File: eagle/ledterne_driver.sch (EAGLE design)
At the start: 15 parts, among them IC1 MEGA8-AI

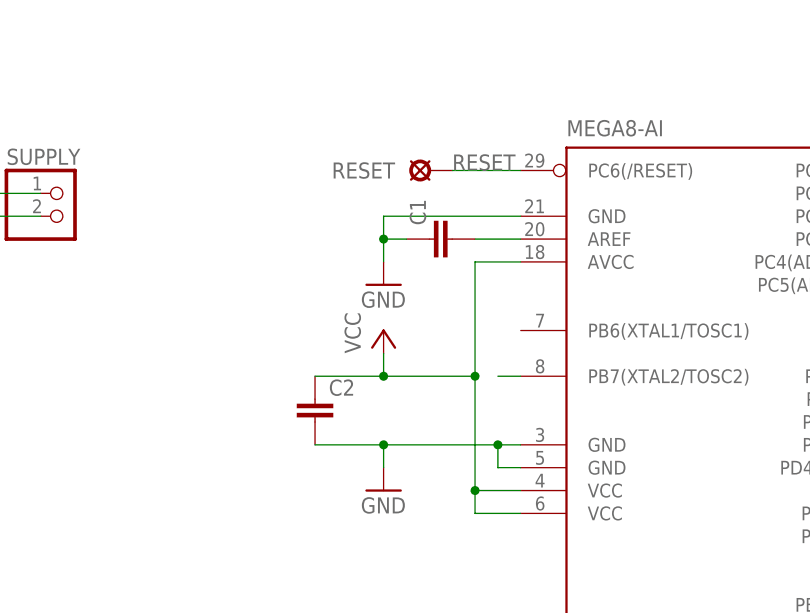
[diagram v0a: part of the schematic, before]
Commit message: Add capacitor values
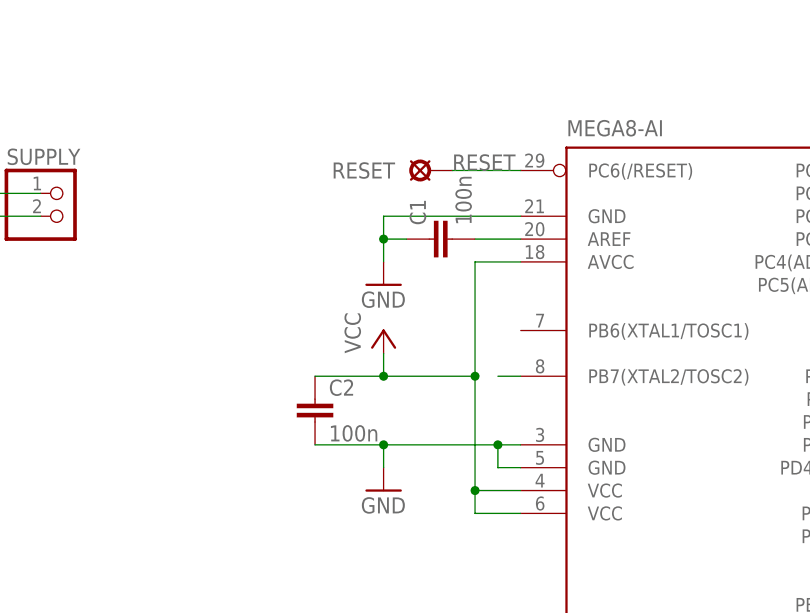
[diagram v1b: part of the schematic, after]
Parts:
- C1, C2: value (none) -> 100n
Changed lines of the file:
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@@
 <part name="GND3" library="supply1" deviceset="GND" device=""/>
 <part name="P+1" library="supply1" deviceset="VCC" device=""/>
-<part name="C1" library="rcl" deviceset="C-EU" device="C0603K"/>
+<part name="C1" library="rcl" deviceset="C-EU" device="C0603K" value="100n"/>
 <part name="GND4" library="supply1" deviceset="GND" device=""/>
 <part name="GND5" library="supply1" deviceset="GND" device=""/>
@@
 <part name="GND7" library="supply1" deviceset="GND" device=""/>
 <part name="GND8" library="supply1" deviceset="GND" device=""/>
-<part name="C2" library="rcl" deviceset="C-EU" device="C0603K"/>
+<part name="C2" library="rcl" deviceset="C-EU" device="C0603K" value="100n"/>
 <part name="JP1" library="pinhead_round_pads" deviceset="PINHD-1X4" device="/90"/>
 <part name="JP2" library="pinhead_round_pads" deviceset="PINHD-1X4" device="/90"/>

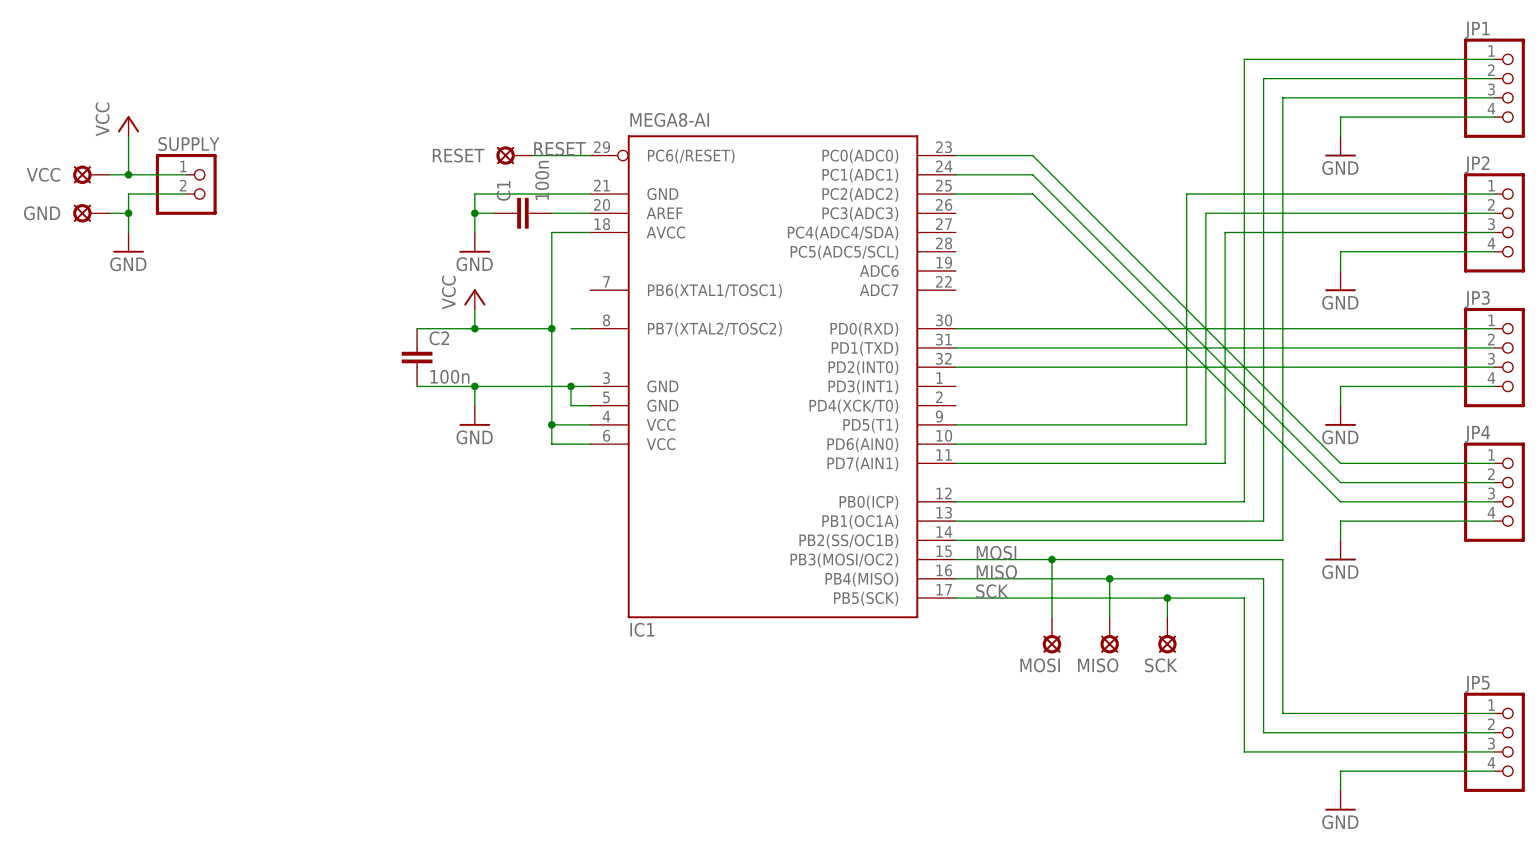
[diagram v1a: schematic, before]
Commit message: Clean up the schematic a little
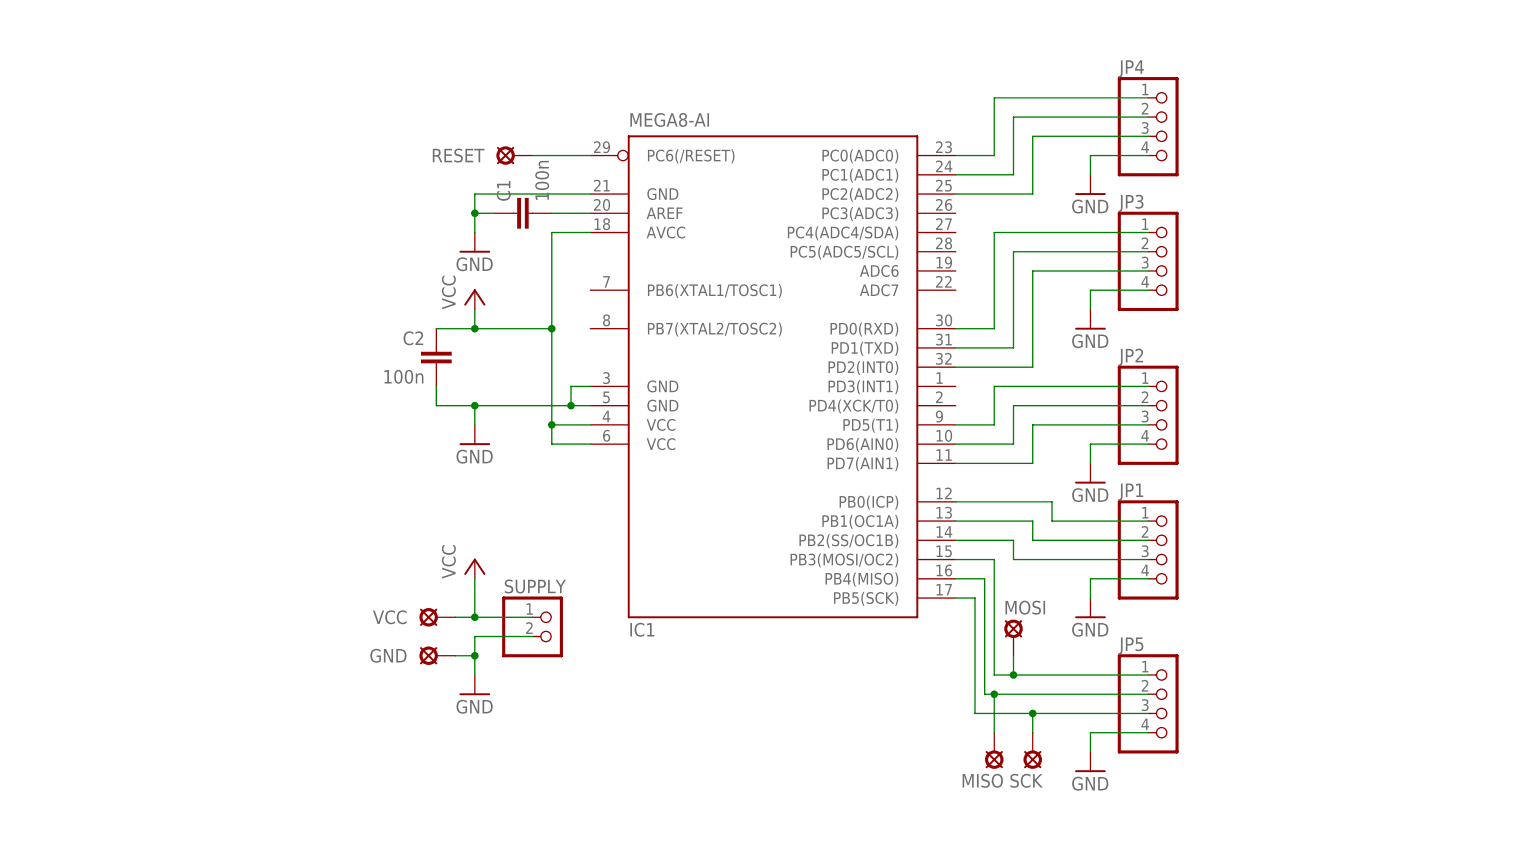
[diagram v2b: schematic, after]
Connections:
- removed net N$14: IC1.PB7(XTAL2/TOSC2)
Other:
- moved on the sheet: C2, GND, JP1, JP2, JP3, JP4, JP5, MISO, MOSI, SCK, SUPPLY, VCC

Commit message: Replace ISP solder pads with through-hole pins
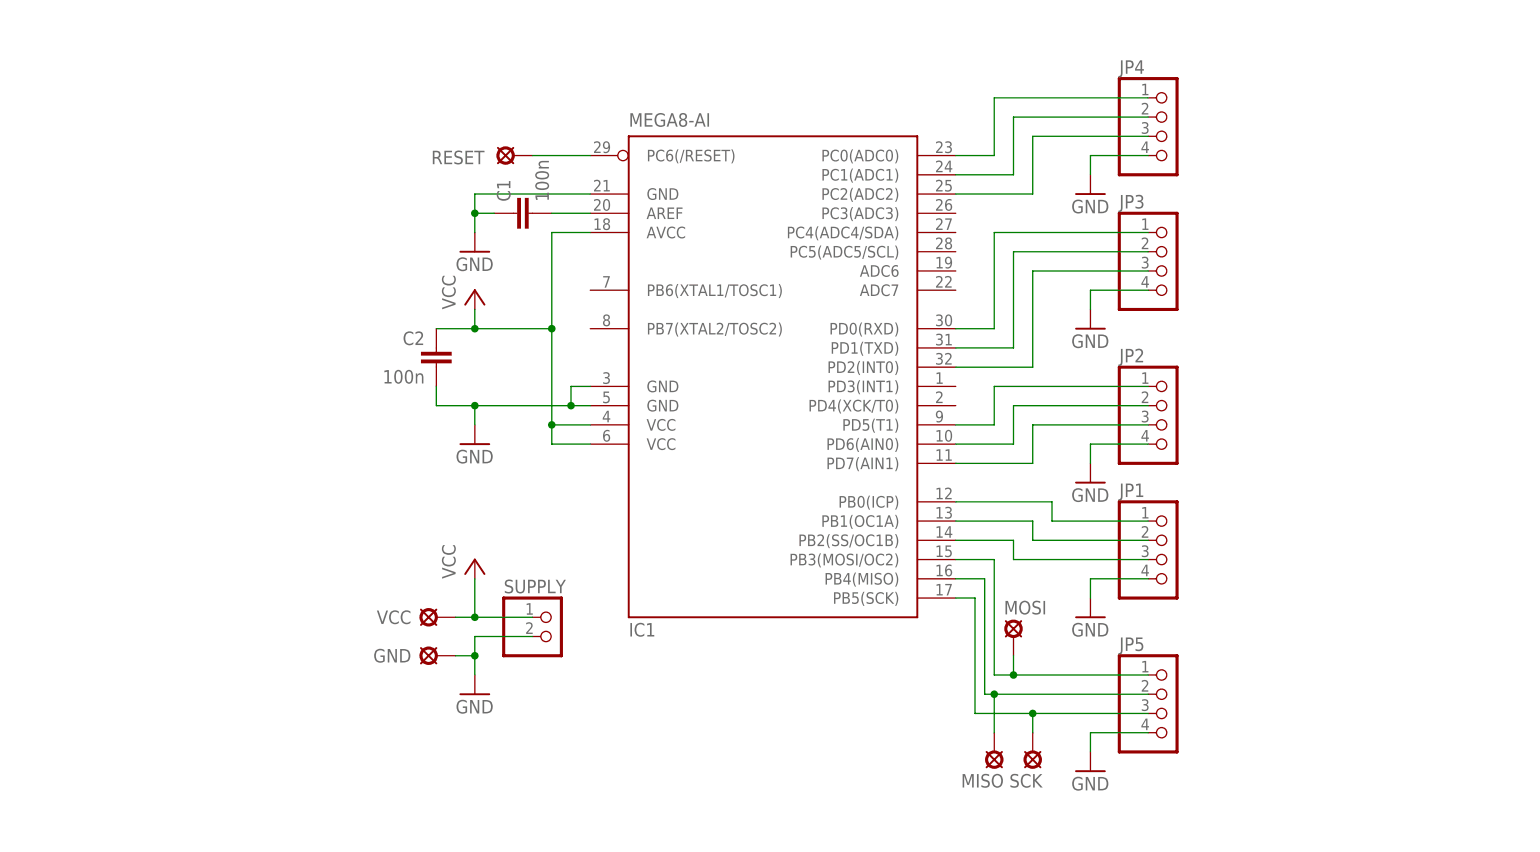
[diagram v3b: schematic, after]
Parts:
- GND, MISO, MOSI, RESET, SCK, VCC: value SOLPAD-SMD-NORMAL -> LSP10; device solpad-smd:SOLPAD-SMD-NORMAL -> solpad-ledterne:LSP10
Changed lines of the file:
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@@
 <part name="P+3" library="supply1" deviceset="VCC" device=""/>
 <part name="GND9" library="supply1" deviceset="GND" device=""/>
-<part name="GND" library="solpad-smd" deviceset="SOLPAD-SMD-NORMAL" device=""/>
-<part name="SCK" library="solpad-smd" deviceset="SOLPAD-SMD-NORMAL" device=""/>
-<part name="MISO" library="solpad-smd" deviceset="SOLPAD-SMD-NORMAL" device=""/>
-<part name="MOSI" library="solpad-smd" deviceset="SOLPAD-SMD-NORMAL" device=""/>
-<part name="RESET" library="solpad-smd" deviceset="SOLPAD-SMD-NORMAL" device=""/>
-<part name="VCC" library="solpad-smd" deviceset="SOLPAD-SMD-NORMAL" device=""/>
+<part name="RESET" library="solpad-ledterne" deviceset="LSP10" device=""/>
+<part name="VCC" library="solpad-ledterne" deviceset="LSP10" device=""/>
+<part name="GND" library="solpad-ledterne" deviceset="LSP10" device=""/>
+<part name="MISO" library="solpad-ledterne" deviceset="LSP10" device=""/>
+<part name="SCK" library="solpad-ledterne" deviceset="LSP10" device=""/>
+<part name="MOSI" library="solpad-ledterne" deviceset="LSP10" device=""/>
 </parts>
 <sheets>
@@
 <instance part="P+3" gate="VCC" x="38.1" y="63.5"/>
 <instance part="GND9" gate="1" x="38.1" y="45.72"/>
-<instance part="GND" gate="1" x="33.02" y="50.8" smashed="yes" rot="R90">
-<attribute name="NAME" x="29.21" y="51.689" size="1.778" layer="95" rot="R180"/>
-</instance>
-<instance part="SCK" gate="1" x="111.76" y="38.1" rot="R180"/>
-<instance part="MISO" gate="1" x="106.68" y="38.1" rot="R180"/>
-<instance part="MOSI" gate="1" x="109.22" y="53.34"/>
 <instance part="RESET" gate="1" x="43.18" y="116.84" smashed="yes" rot="R90">
-<attribute name="NAME" x="39.37" y="117.729" size="1.778" layer="95" rot="R180"/>
+<attribute name="NAME" x="39.37" y="117.475" size="1.778" layer="95" rot="R180"/>
 </instance>
 <instance part="VCC" gate="1" x="33.02" y="55.88" smashed="yes" rot="R90">
-<attribute name="NAME" x="29.21" y="56.769" size="1.778" layer="95" rot="R180"/>
+<attribute name="NAME" x="29.718" y="56.769" size="1.778" layer="95" rot="R180"/>
 </instance>
+<instance part="GND" gate="1" x="33.02" y="50.8" smashed="yes" rot="R90">
+<attribute name="NAME" x="29.718" y="51.689" size="1.778" layer="95" rot="R180"/>
+</instance>
+<instance part="MISO" gate="1" x="106.68" y="38.1" rot="R180"/>
+<instance part="SCK" gate="1" x="111.76" y="38.1" rot="R180"/>
+<instance part="MOSI" gate="1" x="109.22" y="53.34"/>
 </instances>
 <busses>
@@
 <pinref part="GND9" gate="1" pin="GND"/>
 <wire x1="38.1" y1="53.34" x2="38.1" y2="50.8" width="0.1524" layer="91"/>
-<wire x1="38.1" y1="50.8" x2="35.56" y2="50.8" width="0.1524" layer="91"/>
-<pinref part="GND" gate="1" pin="MP"/>
 <wire x1="38.1" y1="50.8" x2="38.1" y2="48.26" width="0.1524" layer="91"/>
 <junction x="38.1" y="50.8"/>
+<pinref part="GND" gate="1" pin="MP"/>
+<wire x1="35.56" y1="50.8" x2="38.1" y2="50.8" width="0.1524" layer="91"/>
 </segment>
 </net>
@@
 <pinref part="SUPPLY" gate="G$1" pin="1"/>
 <wire x1="38.1" y1="55.88" x2="45.72" y2="55.88" width="0.1524" layer="91"/>
+<junction x="38.1" y="55.88"/>
 <pinref part="VCC" gate="1" pin="MP"/>
 <wire x1="35.56" y1="55.88" x2="38.1" y2="55.88" width="0.1524" layer="91"/>
-<junction x="38.1" y="55.88"/>
 </segment>
 </net>
@@
 <wire x1="106.68" y1="63.5" x2="106.68" y2="48.26" width="0.1524" layer="91"/>
 <pinref part="JP5" gate="A" pin="1"/>
-<pinref part="MOSI" gate="1" pin="MP"/>
 <wire x1="106.68" y1="48.26" x2="109.22" y2="48.26" width="0.1524" layer="91"/>
 <wire x1="109.22" y1="48.26" x2="127" y2="48.26" width="0.1524" layer="91"/>
+<junction x="109.22" y="48.26"/>
+<pinref part="MOSI" gate="1" pin="MP"/>
 <wire x1="109.22" y1="50.8" x2="109.22" y2="48.26" width="0.1524" layer="91"/>
-<junction x="109.22" y="48.26"/>
 </segment>
 </net>
@@
 <wire x1="105.41" y1="60.96" x2="105.41" y2="45.72" width="0.1524" layer="91"/>
 <wire x1="105.41" y1="45.72" x2="106.68" y2="45.72" width="0.1524" layer="91"/>
-<wire x1="106.68" y1="45.72" x2="106.68" y2="40.64" width="0.1524" layer="91"/>
 <pinref part="JP5" gate="A" pin="2"/>
-<pinref part="MISO" gate="1" pin="MP"/>
 <wire x1="106.68" y1="45.72" x2="127" y2="45.72" width="0.1524" layer="91"/>
 <junction x="106.68" y="45.72"/>
+<pinref part="MISO" gate="1" pin="MP"/>
+<wire x1="106.68" y1="40.64" x2="106.68" y2="45.72" width="0.1524" layer="91"/>
 </segment>
 </net>
@@
 <wire x1="104.14" y1="58.42" x2="104.14" y2="43.18" width="0.1524" layer="91"/>
 <pinref part="JP5" gate="A" pin="3"/>
-<pinref part="SCK" gate="1" pin="MP"/>
 <wire x1="104.14" y1="43.18" x2="111.76" y2="43.18" width="0.1524" layer="91"/>
 <wire x1="111.76" y1="43.18" x2="127" y2="43.18" width="0.1524" layer="91"/>
+<junction x="111.76" y="43.18"/>
+<pinref part="SCK" gate="1" pin="MP"/>
 <wire x1="111.76" y1="40.64" x2="111.76" y2="43.18" width="0.1524" layer="91"/>
-<junction x="111.76" y="43.18"/>
 </segment>
 </net>

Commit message: Switch to a slightly larger capacitor package
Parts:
- C1, C2: device rcl:C-EUC0603K -> rcl:C-EUC0805K
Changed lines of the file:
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@@
 <part name="GND3" library="supply1" deviceset="GND" device=""/>
 <part name="P+1" library="supply1" deviceset="VCC" device=""/>
-<part name="C1" library="rcl" deviceset="C-EU" device="C0603K" value="100n"/>
+<part name="C1" library="rcl" deviceset="C-EU" device="C0805K" value="100n"/>
 <part name="GND4" library="supply1" deviceset="GND" device=""/>
 <part name="GND5" library="supply1" deviceset="GND" device=""/>
@@
 <part name="GND7" library="supply1" deviceset="GND" device=""/>
 <part name="GND8" library="supply1" deviceset="GND" device=""/>
-<part name="C2" library="rcl" deviceset="C-EU" device="C0603K" value="100n"/>
+<part name="C2" library="rcl" deviceset="C-EU" device="C0805K" value="100n"/>
 <part name="JP1" library="pinhead_round_pads" deviceset="PINHD-1X4" device="/90"/>
 <part name="JP2" library="pinhead_round_pads" deviceset="PINHD-1X4" device="/90"/>
